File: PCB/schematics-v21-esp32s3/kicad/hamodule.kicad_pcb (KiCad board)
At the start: 2 copper layers, 78.4 x 84.3 mm, 91 parts, among them J1 GND|5V, J10 Conn_01x02_Male, J11 2604-1104, J12 2604-1104, J13 EspSense, J2 Conn_01x02_Male, J3 2604-1102, J4 USB | PS, J5 GND|3.3V, J6 Conn_01x02_Male, J7 Current Jumper, J8 USB_C_Receptacle_USB2.0, J9 EspRelays, K1 AQG12205, K2 AQG12205, K3 AQG12205, K4 AQG12205, SW1 Switch, SW2 Switch, U1 LD1117AV33, U2 ESP32-S3-WROOM-2, U3 USBLC6-2SC6, U4 ULN2003A, U5 LDA210-PDIP, U6 LDA210-PDIP, U7 SHT4x

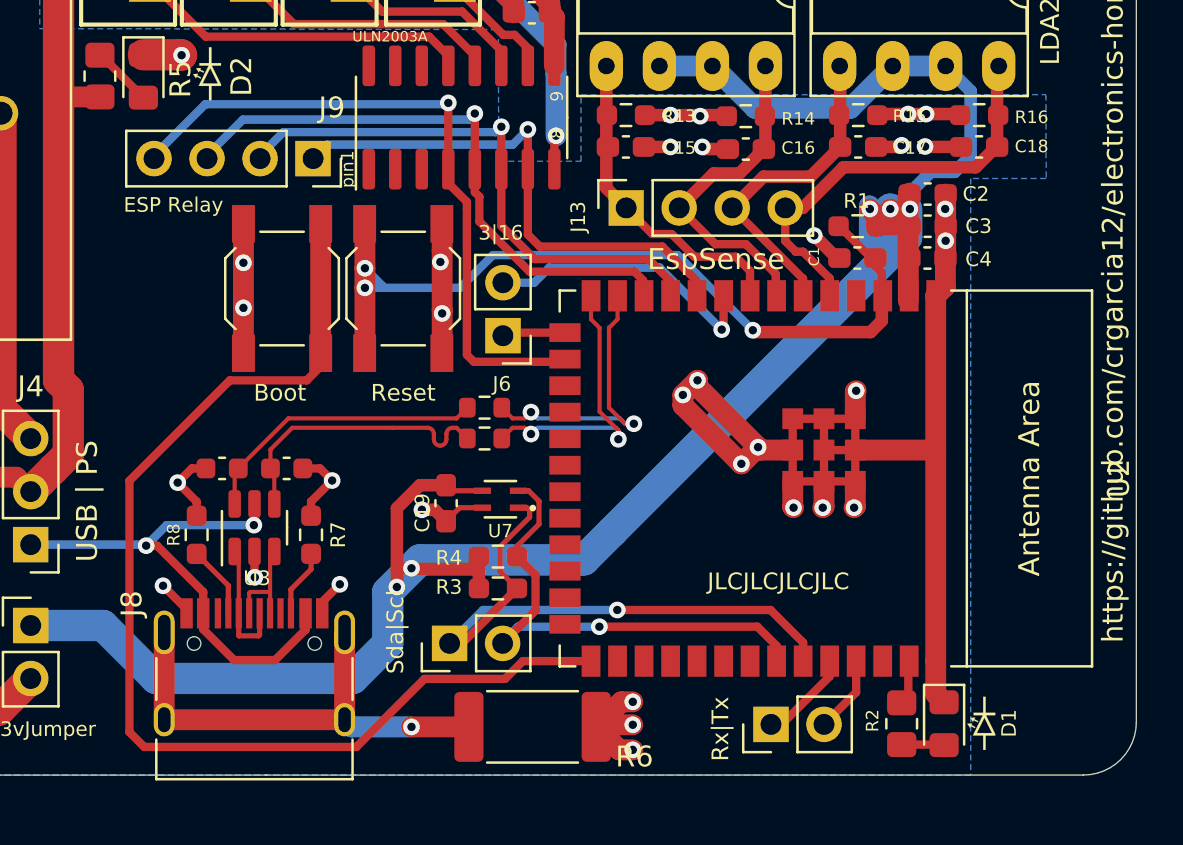
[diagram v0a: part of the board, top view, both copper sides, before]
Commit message: [V21] Bring DEPSI back!; expose 3rd GPIO; remove ESP unused libraries;
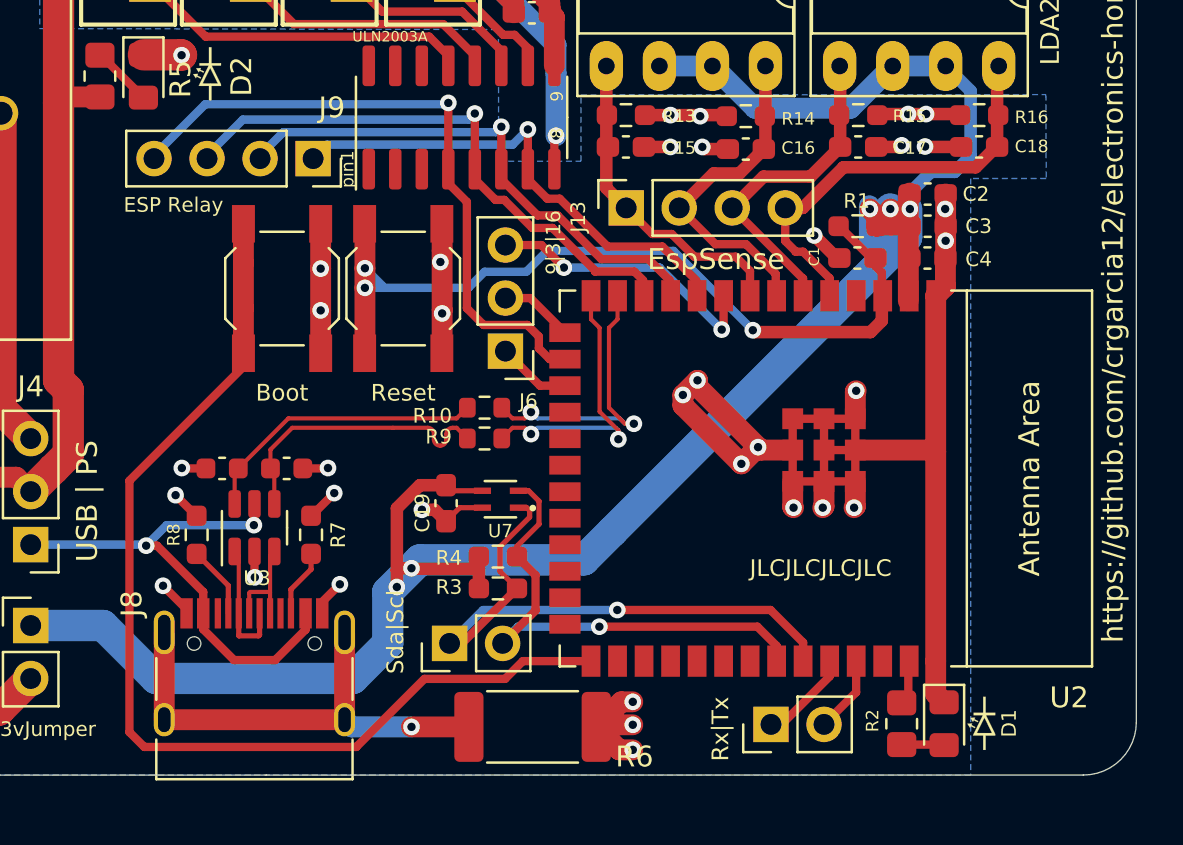
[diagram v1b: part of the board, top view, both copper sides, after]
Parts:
- removed G5: LOGO, icons:depsi
- added G***: LOGO, icons:depsi, B.Cu at (97.1, 99.9)
- J6: footprint Connector_PinHeader_2.54mm:PinHeader_1x02_P2.54mm_Vertical -> Connector_PinHeader_2.54mm:PinHeader_1x03_P2.54mm_Vertical
- moved J6 0.75 mm to (79.0, 95.2)
- turned SW2 to 90 degrees
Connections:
- J6 pad 1: GPIO3 -> GPIO9
- J6 pad 2: GPIO16 -> GPIO3
- U2 pad 17: unconnected-(U2-Pad17) -> GPIO9
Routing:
- net IO0: track 54.4 -> 50.7 mm
- net GPIO9: track 0.00 -> 3.54 mm
- net GND: track 168.4 -> 166.5 mm, vias 40 -> 42
- net EspRel4: track 25.9 -> 24.3 mm
- net EspRel3: track 27.1 -> 25.7 mm
- net EspRel2: track 29.0 -> 27.9 mm
- net EspRel1: track 32.5 -> 31.4 mm
- net GPIO3: track 3.03 -> 3.54 mm
- net GPIO16: vias 1 -> 2

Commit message: Images + Gerbers
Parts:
- removed G7: LOGO, icons:paula
- added D3: BAT60A, Diode_SMD:D_SOD-323, F.Cu at (61.0, 104.5)
- R3: renamed from R9; value 22r -> 22Ω
- R4: renamed from R10; value 22r -> 22Ω
- renumbered C5 to C4, C4 to C5, D2 to D1, D1 to D2, G*** to G5, J8 to J11, J3 to J2, J2 to J3, J6 to J5, J5 to J6, J9 to J8, J11 to J9, R8 to R10, R13 to R11, R14 to R12, R15 to R13, R16 to R14, R17 to R15, R18 to R16, R19 to R17, R20 to R18, R21 to R19, R5 to R2, R22 to R20, R23 to R21, R24 to R22, R2 to R5, R3 to R6, R4 to R7, R6 to R8, R7 to R9, U4 to U3, U3 to U4
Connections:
- J11 pad A4: VBUS -> Net-(D3-Pad2)
- J11 pad A9: VBUS -> Net-(D3-Pad2)
- J11 pad B4: VBUS -> Net-(D3-Pad2)
- J11 pad B9: VBUS -> Net-(D3-Pad2)
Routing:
- net Net-(D3-Pad2): track 0.00 -> 12.0 mm
- net VBUS: track 24.5 -> 13.3 mm
